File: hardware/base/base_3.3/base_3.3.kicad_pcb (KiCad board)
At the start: 2 copper layers, 77 x 17 mm, 9 parts, among them IC1 single_pad_smd, IC2 single_pad_smd, J1 Conn 1, J2 Conn 2

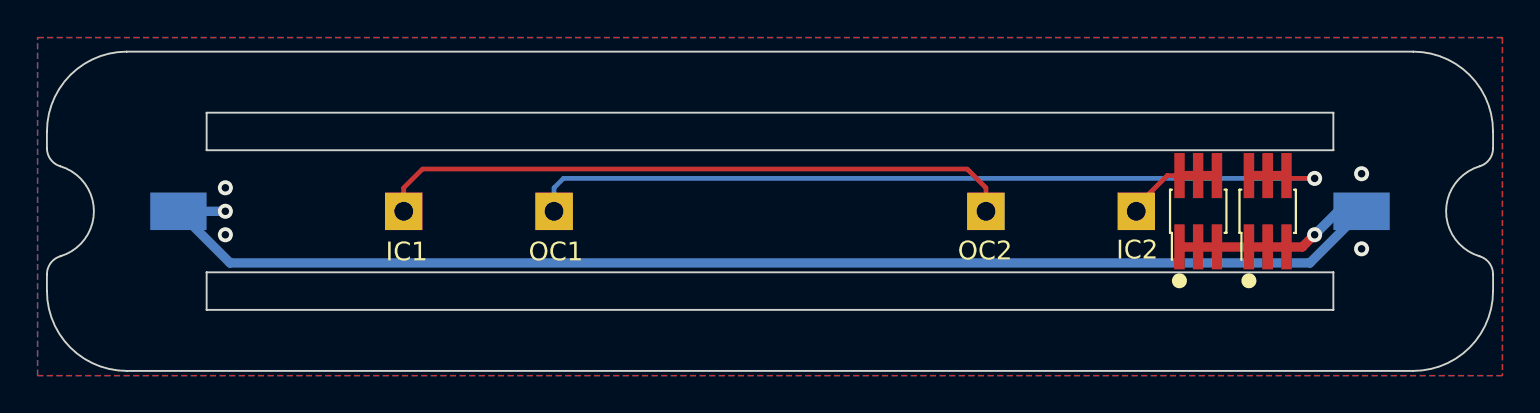
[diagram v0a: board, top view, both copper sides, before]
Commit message: Upgrade to Kicad 6
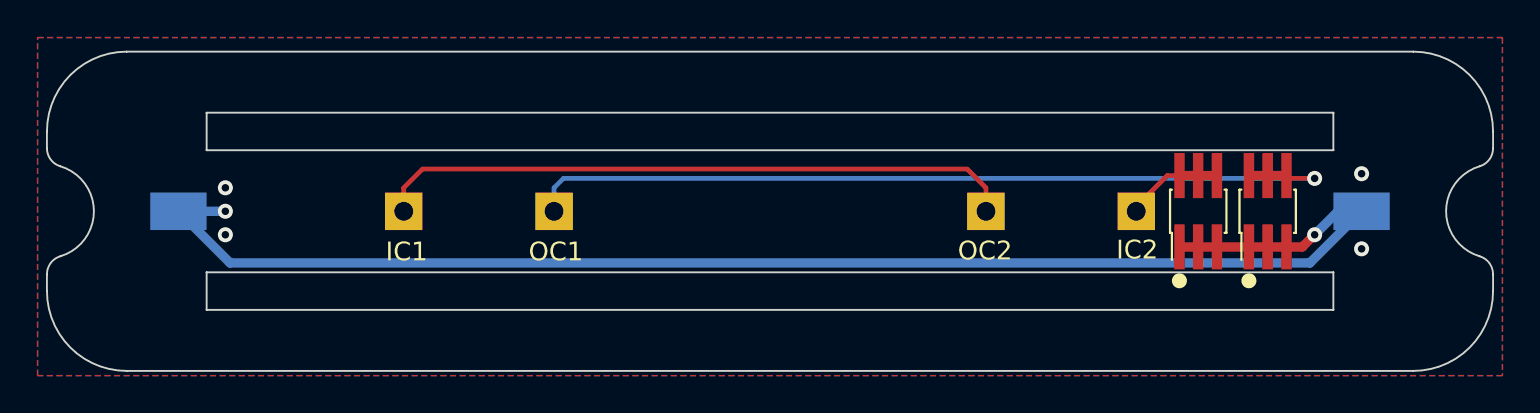
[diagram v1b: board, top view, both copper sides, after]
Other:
- outline, holes or cut-outs redrawn
- net class Default removed

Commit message: Base 3.3 updated to v2
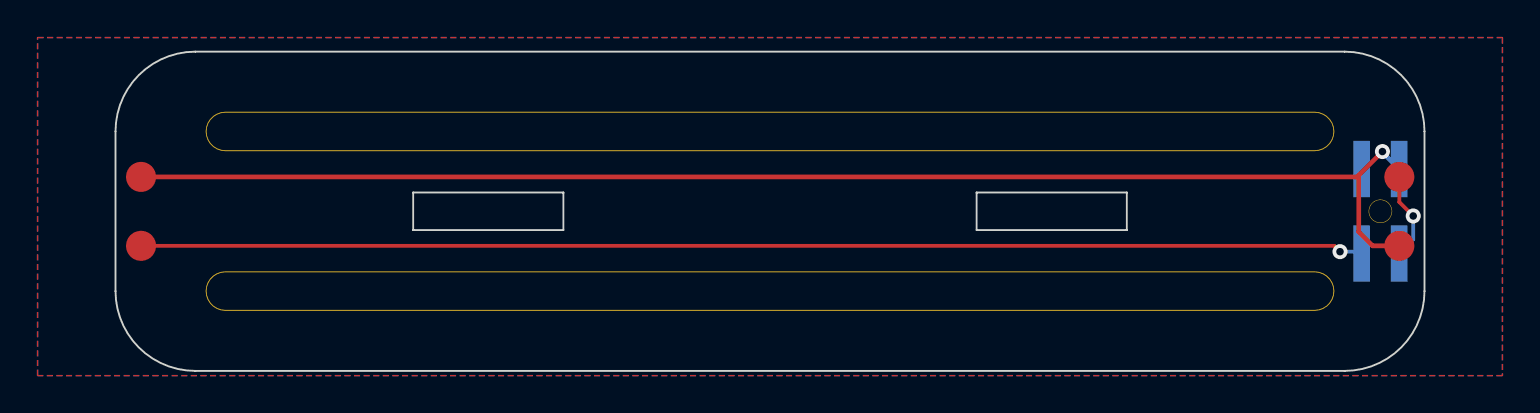
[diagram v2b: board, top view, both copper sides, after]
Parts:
- removed GND (x2): single_pad_smd, cycfi_library:single-pad-3x2
- removed J2: Conn 2, cycfi_library:pin_header_2x3p_1.00mm_smd_vertical
- added H5: single_pad, xr_spectra_library:rail_slot_3.3, F.Cu at (125.0, 51.0)
- added H6: single_pad, xr_spectra_library:rail_slot_3.3, F.Cu at (125.0, 59.5)
- IC1, IC2, OC1, OC2: value single_pad_smd -> single_pad; footprint cycfi_library:single-pad-2x2-th -> cycfi_library:single-pad-1.6x1.6_circular; moved to F.Cu
- J1: value Conn 1 -> conn_2x2; footprint cycfi_library:pin_header_2x3p_1.00mm_smd_vertical -> cycfi_library:pin_header_2x2p_2.00mm_smd_vertical; moved to B.Cu
- moved OC1 45.0 mm to (158.5, 53.4), turned to 180 degrees
- moved OC2 45.0 mm to (91.5, 57.1), turned to 180 degrees
- moved IC2 14.1 mm to (158.5, 57.1), turned to 180 degrees
- moved IC1 14.1 mm to (91.5, 53.4), turned to 180 degrees
- moved J1 6.00 mm to (157.5, 55.2)
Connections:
- IC1 pad 1: /ic1 -> inner_coil
- IC2 pad 1: /ic2 -> inner_coil
- J1 pad 1: GND -> inner_coil
- J1 pad 3: GND -> /out-
- J1 pad 4: /oc1 -> /out+
- OC1 pad 1: /oc1 -> /out+
- OC2 pad 1: /ic1 -> /out-
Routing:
- net GND: track 78.3 -> 0.00 mm, vias 6 -> 0
- net inner_coil: track 0.00 -> 73.4 mm, vias 0 -> 1
- net /out-: track 0.00 -> 65.2 mm, vias 0 -> 1
- net /oc1: track 45.5 -> 0.00 mm, vias 1 -> 0
- net /ic1: track 34.3 -> 0.00 mm
- net /ic2: track 5.23 -> 0.00 mm
- net /out+: track 0.00 -> 4.70 mm, vias 0 -> 1
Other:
- board size 77 x 17 mm -> 69.7 x 17 mm
- board text removed: "IC1"
- board text removed: "IC2"
- board text removed: "OC1"
- board text removed: "OC2"

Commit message: Copied 3.3 to 3.5 and 4.0
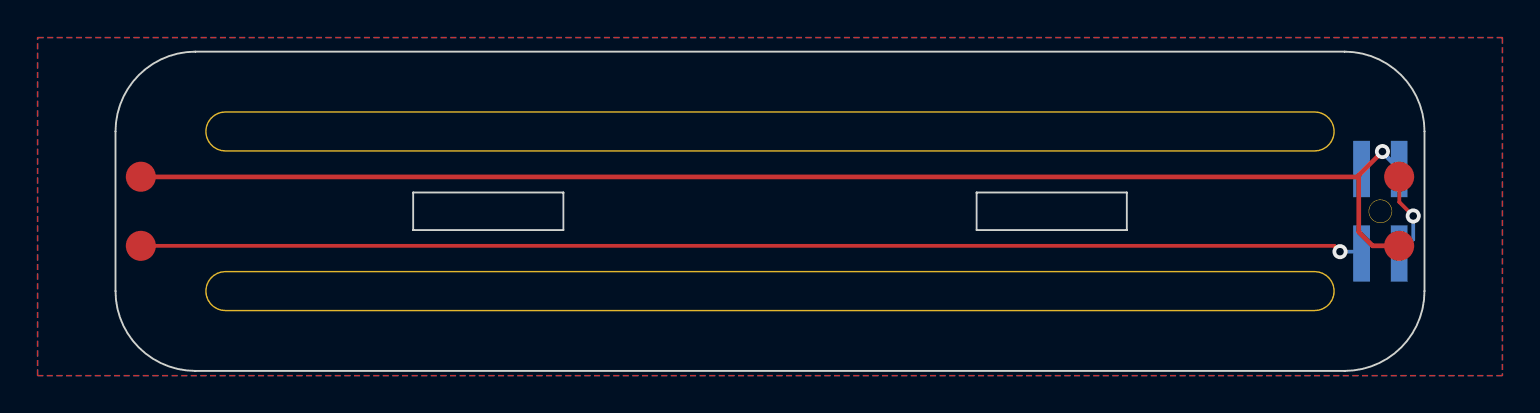
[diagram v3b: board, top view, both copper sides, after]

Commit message: 3.3" updated PCB layout from solidworks model
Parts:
- moved OC1 0.19 mm to (158.6, 53.3)
- moved IC1 0.18 mm to (91.4, 53.3)
- moved IC2 0.18 mm to (158.6, 57.2)
- moved OC2 0.18 mm to (91.4, 57.2)

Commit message: WIP
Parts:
- G***: moved to F.Cu
- moved IC2 67.3 mm to (91.4, 52.8), turned to 0 degrees
- moved OC2 67.3 mm to (158.6, 52.8), turned to 0 degrees
- moved OC1 67.3 mm to (91.4, 56.7), turned to 0 degrees
- moved IC1 67.3 mm to (158.6, 56.7), turned to 0 degrees
- moved J1 65.0 mm to (92.5, 54.8), turned to -90 degrees
- moved H6 9.00 mm to (125.0, 50.5), turned to 180 degrees
- moved H5 8.00 mm to (125.0, 59.0), turned to 180 degrees
- moved G*** 0.71 mm to (124.8, 54.8), turned to 0 degrees
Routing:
- net inner_coil: track 73.7 -> 0.00 mm, vias 1 -> 0
- net /out-: track 65.2 -> 0.00 mm, vias 1 -> 0
- net /out+: track 4.82 -> 0.00 mm, vias 1 -> 0

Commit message: fixed schematics
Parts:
- renumbered IC2 to IC1, IC1 to IC2, OC2 to OC1, OC1 to OC2
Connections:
- IC1 pad 1: inner_coil -> /out+
- IC2 pad 1: inner_coil -> /out-
- J1 pad 1: inner_coil -> middle_coil
- OC1 pad 1: /out- -> middle_coil
- OC2 pad 1: /out+ -> middle_coil
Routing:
- net middle_coil: track 0.00 -> 79.0 mm, vias 0 -> 2
- net /out-: track 0.00 -> 69.6 mm, vias 0 -> 1
- net /out+: track 0.00 -> 2.74 mm, vias 0 -> 1
- net GND: vias 0 -> 4
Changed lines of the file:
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@@
   (net 0 "")
   (net 1 "GND")
-  (net 2 "inner_coil")
+  (net 2 "middle_coil")
   (net 3 "/out-")
   (net 4 "/out+")
@@
     (property "Sheetname" "")
     (attr smd)
-    (fp_text reference "IC2" (at -2.65 -0.26) (layer "F.SilkS")
+    (fp_text reference "IC1" (at -2.65 -0.26) (layer "F.SilkS")
       (effects (font (size 1 1) (thickness 0.15)))
     )
@@
     )
     (pad "1" smd circle (at 0 0) (size 1.6 1.6) (layers "F.Cu" "F.Paste" "F.Mask")
-      (net 2 "inner_coil") (pinfunction "1") (pintype "input"))
+      (net 4 "/out+") (pinfunction "1") (pintype "input"))
   )
   (footprint "cycfi_library:single-pad-1.6x1.6_circular" (layer "F.Cu")
@@
     (property "Sheetname" "")
     (attr smd)
-    (fp_text reference "OC2" (at 3.15 -0.01) (layer "F.SilkS")
+    (fp_text reference "OC1" (at 3.15 -0.01) (layer "F.SilkS")
       (effects (font (size 1 1) (thickness 0.15)))
     )
@@
     )
     (pad "1" smd circle (at 0 0) (size 1.6 1.6) (layers "F.Cu" "F.Paste" "F.Mask")
-      (net 3 "/out-") (pinfunction "1") (pintype "input"))
+      (net 2 "middle_coil") (pinfunction "1") (pintype "input"))
   )
   (footprint "cycfi_library:cycfi-logo-15mm" locked (layer "F.Cu")
@@
     (property "Sheetname" "")
     (attr smd)
-    (fp_text reference "OC1" (at -2.89 0.26) (layer "F.SilkS")
+    (fp_text reference "OC2" (at -2.89 0.26) (layer "F.SilkS")
       (effects (font (size 1 1) (thickness 0.15)))
     )
@@
     )
     (pad "1" smd circle (at 0 0) (size 1.6 1.6) (layers "F.Cu" "F.Paste" "F.Mask")
-      (net 4 "/out+") (pinfunction "1") (pintype "input"))
+      (net 2 "middle_coil") (pinfunction "1") (pintype "input"))
   )
   (footprint "cycfi_library:single-pad-1.6x1.6_circular" (layer "F.Cu")
@@
     (property "Sheetname" "")
     (attr smd)
-    (fp_text reference "IC1" (at 2.9 0.01) (layer "F.SilkS")
+    (fp_text reference "IC2" (at 2.9 0.01) (layer "F.SilkS")
       (effects (font (size 1 1) (thickness 0.15)))
     )
@@
     )
     (pad "1" smd circle (at 0 0) (size 1.6 1.6) (layers "F.Cu" "F.Paste" "F.Mask")
-      (net 2 "inner_coil") (pinfunction "1") (pintype "input"))
+      (net 3 "/out-") (pinfunction "1") (pintype "input"))
   )
   (footprint "xr_spectra_library:rail_slot_3.3" (layer "F.Cu")
@@
       (effects (font (size 1 1) (thickness 0.15)))
     )
-    (fp_text value "single_pad" (at 0 3 180 unlocked) (layer "F.Fab")
+    (fp_text value "single_pad" (at 0 3 unlocked) (layer "F.Fab")
       (effects (font (size 1 1) (thickness 0.15)))
     )
@@
       (effects (font (size 1 1) (thickness 0.15)))
     )
-    (fp_text value "single_pad" (at 0 3 180 unlocked) (layer "F.Fab")
+    (fp_text value "single_pad" (at 0 3 unlocked) (layer "F.Fab")
       (effects (font (size 1 1) (thickness 0.15)))
     )
@@
     (pad "" np_thru_hole circle (at 0 0 270) (size 1.25 1.25) (drill 1.2) (layers F&B.Cu *.Mask))
     (pad "1" smd rect (at 2.25 1 270) (size 3 0.89) (layers "B.Cu" "B.Paste" "B.Mask")
-      (net 2 "inner_coil") (pinfunction "Pin_1") (pintype "passive"))
+      (net 2 "middle_coil") (pinfunction "Pin_1") (pintype "passive"))
     (pad "2" smd rect (at 2.25 -1 270) (size 3 0.89) (layers "B.Cu" "B.Paste" "B.Mask")
       (net 1 "GND") (pinfunction "Pin_2") (pintype "passive"))
@@
   (gr_arc (start 94.4 63.25) (mid 91.394796 62.005204) (end 90.15 59) (layer "Edge.Cuts") (width 0.1))
   (gr_line (start 144 53.75) (end 136 53.75) (layer "Edge.Cuts") (width 0.1))
+  (via (at 96.25 61.75) (size 0.8) (drill 0.4) (layers "F.Cu" "B.Cu") (free) (net 1))
+  (via (at 94.25 61.75) (size 0.8) (drill 0.4) (layers "F.Cu" "B.Cu") (free) (net 1))
+  (via (at 152.5 61.75) (size 0.8) (drill 0.4) (layers "F.Cu" "B.Cu") (free) (net 1))
+  (via (at 154.5 61.75) (size 0.8) (drill 0.4) (layers "F.Cu" "B.Cu") (free) (net 1))
+  (segment (start 155.92452 60.82548) (end 93.32548 60.82548) (width 0.25) (layer "F.Cu") (net 2))
+  (segment (start 92.15 57.5) (end 91.39 56.74) (width 0.25) (layer "F.Cu") (net 2))
+  (segment (start 158.6 52.76) (end 155.92452 55.43548) (width 0.25) (layer "F.Cu") (net 2))
+  (segment (start 155.92452 55.43548) (end 155.92452 60.82548) (width 0.25) (layer "F.Cu") (net 2))
+  (segment (start 93.32548 60.82548) (end 93.07548 60.82548) (width 0.25) (layer "F.Cu") (net 2))
+  (segment (start 92.455498 57.5) (end 92.15 57.5) (width 0.25) (layer "F.Cu") (net 2))
+  (segment (start 93.07548 60.82548) (end 91.5 59.25) (width 0.25) (layer "F.Cu") (net 2))
+  (via (at 91.5 59.25) (size 0.8) (drill 0.4) (layers "F.Cu" "B.Cu") (net 2))
+  (via (at 92.455498 57.5) (size 0.8) (drill 0.4) (layers "F.Cu" "B.Cu") (net 2))
+  (segment (start 91.5 57) (end 91.955498 57) (width 0.25) (layer "B.Cu") (net 2))
+  (segment (start 91.5 59.25) (end 91.5 57) (width 0.25) (layer "B.Cu") (net 2))
+  (segment (start 91.955498 57) (end 92.455498 57.5) (width 0.25) (layer "B.Cu") (net 2))
+  (segment (start 158.6 58.15) (end 157.75 59) (width 0.2) (layer "F.Cu") (net 3))
+  (segment (start 158.6 56.74) (end 158.6 58.15) (width 0.2) (layer "F.Cu") (net 3))
+  (via (at 157.75 59) (size 0.8) (drill 0.4) (layers "F.Cu" "B.Cu") (net 3))
+  (segment (start 151.25 52.5) (end 93.5 52.5) (width 0.2) (layer "B.Cu") (net 3))
+  (segment (start 157.75 59) (end 151.25 52.5) (width 0.2) (layer "B.Cu") (net 3))
+  (segment (start 91.4 52.76) (end 91.445498 52.76) (width 0.2) (layer "F.Cu") (net 4))
+  (segment (start 91.445498 52.76) (end 92.455498 51.75) (width 0.2) (layer "F.Cu") (net 4))
+  (via (at 92.455498 51.75) (size 0.8) (drill 0.4) (layers "F.Cu" "B.Cu") (net 4))
+  (segment (start 92.25 51.75) (end 91.5 52.5) (width 0.2) (layer "B.Cu") (net 4))
+  (segment (start 92.455498 51.75) (end 92.25 51.75) (width 0.2) (layer "B.Cu") (net 4))
   (zone (net 1) (net_name "GND") (layer "F.Cu") (hatch edge 0.508)
     (connect_pads yes (clearance 0.508))
     (min_thickness 0.254) (filled_areas_thickness no)
-    (fill (thermal_gap 0.508) (thermal_bridge_width 0.508))
+    (fill yes (thermal_gap 0.508) (thermal_bridge_width 0.508))
     (polygon
       (pts
@@
     (connect_pads yes (clearance 0.508))
     (min_thickness 0.254) (filled_areas_thickness no)
-    (fill (thermal_gap 0.508) (thermal_bridge_width 0.508))
+    (fill yes (thermal_gap 0.508) (thermal_bridge_width 0.508))
     (polygon
       (pts

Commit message: 3.5" and 3.3" good to go
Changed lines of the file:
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@@
     (property "Sheetname" "")
     (attr smd)
-    (fp_text reference "IC1" (at -2.65 -0.26) (layer "F.SilkS")
+    (fp_text reference "IC1" (at -2.65 -0.26) (layer "F.SilkS") hide
       (effects (font (size 1 1) (thickness 0.15)))
     )
@@
     (property "Sheetname" "")
     (attr smd)
-    (fp_text reference "OC1" (at 3.15 -0.01) (layer "F.SilkS")
+    (fp_text reference "OC1" (at 3.15 -0.01) (layer "F.SilkS") hide
       (effects (font (size 1 1) (thickness 0.15)))
     )
@@
     (property "Sheetname" "")
     (attr smd)
-    (fp_text reference "OC2" (at -2.89 0.26) (layer "F.SilkS")
+    (fp_text reference "OC2" (at -2.89 0.26) (layer "F.SilkS") hide
       (effects (font (size 1 1) (thickness 0.15)))
     )
@@
     (property "Sheetname" "")
     (attr smd)
-    (fp_text reference "IC2" (at 2.9 0.01) (layer "F.SilkS")
+    (fp_text reference "IC2" (at 2.9 0.01) (layer "F.SilkS") hide
       (effects (font (size 1 1) (thickness 0.15)))
     )
@@
   (via (at 152.5 61.75) (size 0.8) (drill 0.4) (layers "F.Cu" "B.Cu") (free) (net 1))
   (via (at 154.5 61.75) (size 0.8) (drill 0.4) (layers "F.Cu" "B.Cu") (free) (net 1))
-  (segment (start 155.92452 60.82548) (end 93.32548 60.82548) (width 0.25) (layer "F.Cu") (net 2))
+  (segment (start 93 60.75) (end 91.5 59.25) (width 0.25) (layer "F.Cu") (net 2))
+  (segment (start 158.6 52.76) (end 157 54.36) (width 0.25) (layer "F.Cu") (net 2))
+  (segment (start 156.75 60.75) (end 93 60.75) (width 0.25) (layer "F.Cu") (net 2))
   (segment (start 92.15 57.5) (end 91.39 56.74) (width 0.25) (layer "F.Cu") (net 2))
-  (segment (start 158.6 52.76) (end 155.92452 55.43548) (width 0.25) (layer "F.Cu") (net 2))
-  (segment (start 155.92452 55.43548) (end 155.92452 60.82548) (width 0.25) (layer "F.Cu") (net 2))
-  (segment (start 93.32548 60.82548) (end 93.07548 60.82548) (width 0.25) (layer "F.Cu") (net 2))
+  (segment (start 157 54.36) (end 157 60.5) (width 0.25) (layer "F.Cu") (net 2))
+  (segment (start 157 60.5) (end 156.75 60.75) (width 0.25) (layer "F.Cu") (net 2))
   (segment (start 92.455498 57.5) (end 92.15 57.5) (width 0.25) (layer "F.Cu") (net 2))
-  (segment (start 93.07548 60.82548) (end 91.5 59.25) (width 0.25) (layer "F.Cu") (net 2))
   (via (at 91.5 59.25) (size 0.8) (drill 0.4) (layers "F.Cu" "B.Cu") (net 2))
   (via (at 92.455498 57.5) (size 0.8) (drill 0.4) (layers "F.Cu" "B.Cu") (net 2))

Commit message: fine tuning
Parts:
- IC1: value single_pad -> IC1
- IC2: value single_pad -> IC2
- OC1: value single_pad -> OC1
- OC2: value single_pad -> OC2
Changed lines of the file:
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@@
       (effects (font (size 1 1) (thickness 0.15)))
     )
-    (fp_text value "single_pad" (at 0 -2.54) (layer "F.Fab")
+    (fp_text value "IC1" (at -3.15 -0.01) (layer "F.Fab")
       (effects (font (size 1 1) (thickness 0.15)))
     )
@@
       (effects (font (size 1 1) (thickness 0.15)))
     )
-    (fp_text value "single_pad" (at 0 -2.54) (layer "F.Fab")
+    (fp_text value "OC1" (at 3.15 -0.01) (layer "F.Fab")
       (effects (font (size 1 1) (thickness 0.15)))
     )
@@
       (effects (font (size 1 1) (thickness 0.15)))
     )
-    (fp_text value "single_pad" (at 0 -2.54) (layer "F.Fab")
+    (fp_text value "OC2" (at -3.14 0.11) (layer "F.Fab")
       (effects (font (size 1 1) (thickness 0.15)))
     )
@@
       (effects (font (size 1 1) (thickness 0.15)))
     )
-    (fp_text value "single_pad" (at 0 -2.54) (layer "F.Fab")
-      (effects (font (size 1 1) (thickness 0.15)))
-    )
+    (fp_text value "IC2" (at 3.075 0.01) (layer "F.Fab")
+      (effects (font (size 1 1) (thickness 0.15)))
+    )
